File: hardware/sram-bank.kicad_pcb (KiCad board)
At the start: 2 copper layers, 50.8 x 78.7 mm, 45 parts, among them U1 74LVC138A, U10 74LVC8T245, U11 74LVC8T245, U12 IS66WV51216EALL, U13 74LVC138A, U2 74LVC8T245, U3 74LVC8T245, U4 74LVC8T245, U5 74LVC8T245, U6 74LVC8T245, U7 74LVC8T245, U8 74LVC8T245, U9 74LVC8T245

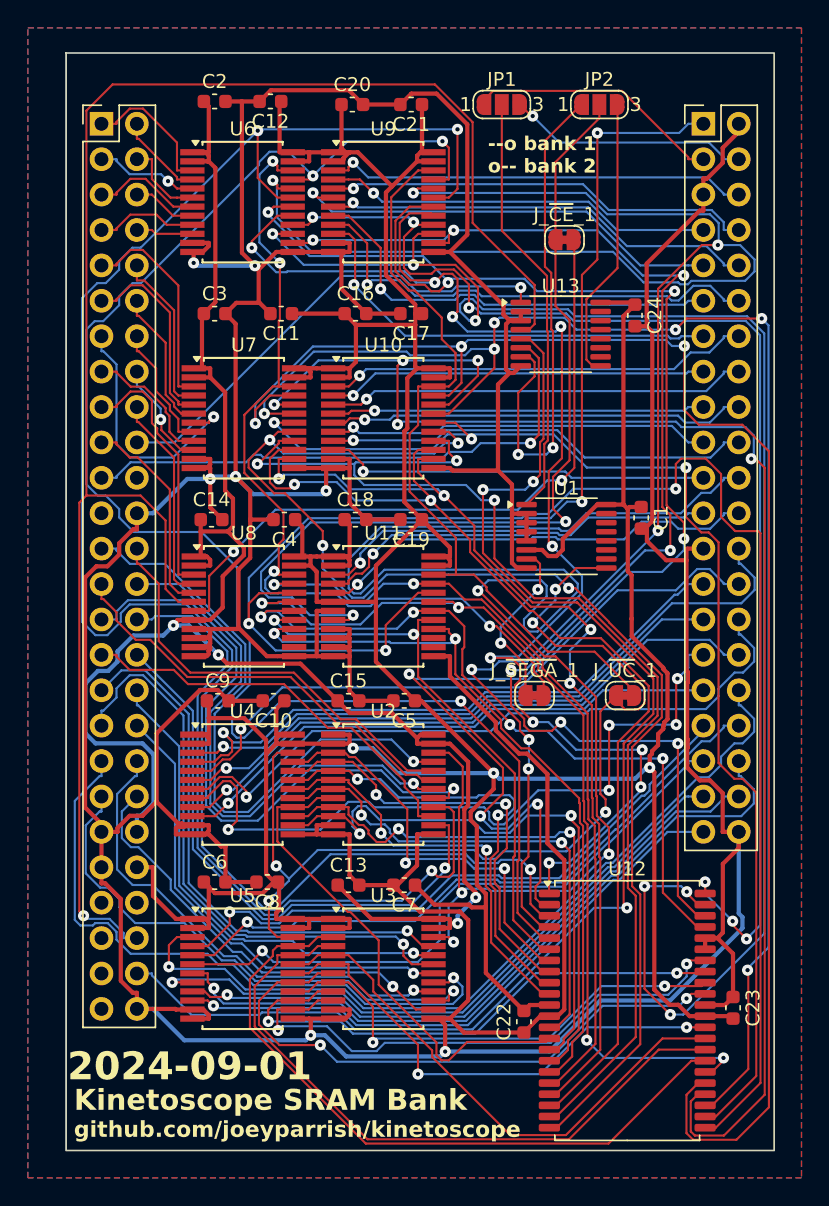
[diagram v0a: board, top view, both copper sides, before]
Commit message: Correct SRAM board debug pads
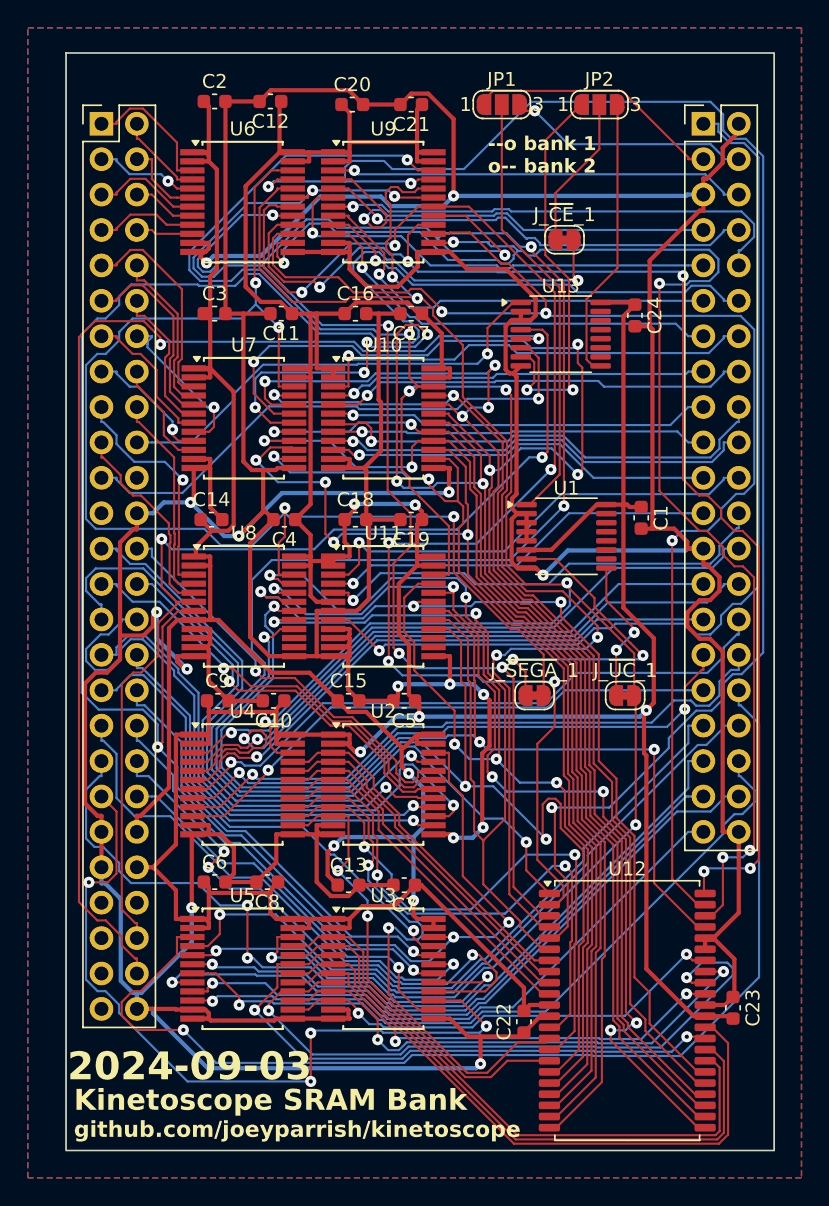
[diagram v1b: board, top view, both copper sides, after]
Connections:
- U2 pad 22: /~{SRAM_CE} -> /~{SRAM_CE_INT}
- U3 pad 22: /~{SRAM_CE} -> /~{SRAM_CE_INT}
- U4 pad 22: /~{UC_CONTROL} -> /~{UC_CONTROL_INT}
- U5 pad 22: /~{UC_CONTROL} -> /~{UC_CONTROL_INT}
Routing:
- net /~{SRAM_CE}: track 136.3 -> 11.0 mm, vias 5 -> 0
- net /~{UC_CONTROL_INT}: track 55.4 -> 172.6 mm, vias 0 -> 8
- net /~{SRAM_CE_INT}: track 49.4 -> 151.7 mm, vias 2 -> 4
- net /~{UC_CONTROL}: track 72.3 -> 10.5 mm, vias 5 -> 2
- net /~{SEGA_CE}: track 123.6 -> 74.1 mm, vias 1 -> 2
- net /SRAM_A17: track 115.7 -> 71.4 mm, vias 3 -> 6
- net /SRAM_A8: track 113.9 -> 74.1 mm, vias 3 -> 2
- net GND: track 503.0 -> 542.8 mm, vias 7 -> 15
- net /SRAM_A4: track 99.3 -> 139.0 mm, vias 10 -> 5
- net /SRAM_A1: track 133.1 -> 93.7 mm, vias 7 -> 4
- net /SRAM_A2: track 129.0 -> 90.6 mm, vias 3 -> 5
- net /~{SEGA_CONTROL_INT}: track 63.7 -> 95.2 mm
- net /~{SRAM_FINAL_WE}: track 53.5 -> 80.5 mm, vias 2 -> 3
- net /SRAM_A9: track 111.3 -> 85.2 mm, vias 5 -> 4
- net /SRAM_A12: track 96.4 -> 71.4 mm, vias 4 -> 2
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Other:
- board text added: "2024-09-03"
- board text removed: "2024-09-01"

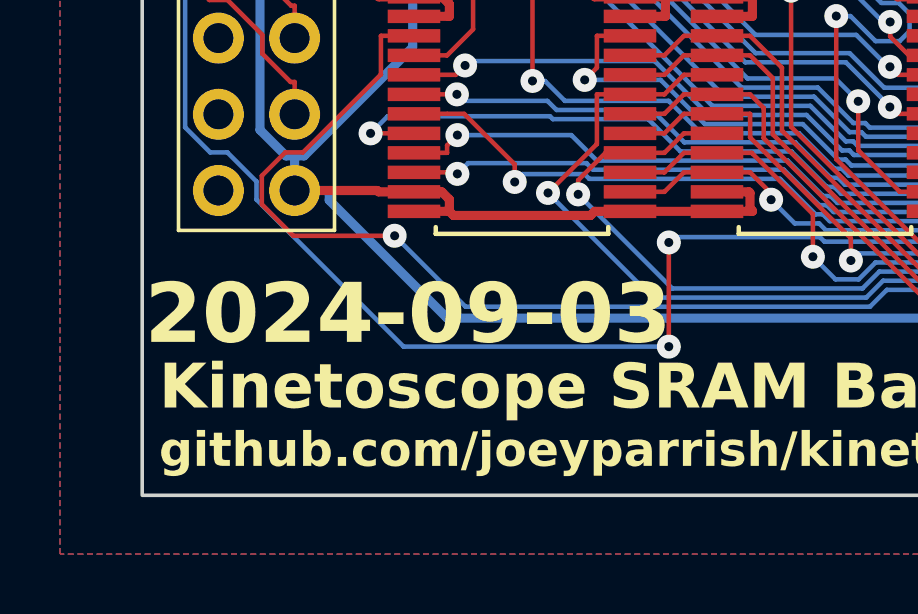
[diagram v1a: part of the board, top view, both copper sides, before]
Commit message: Fix footprint for new SMD regulator
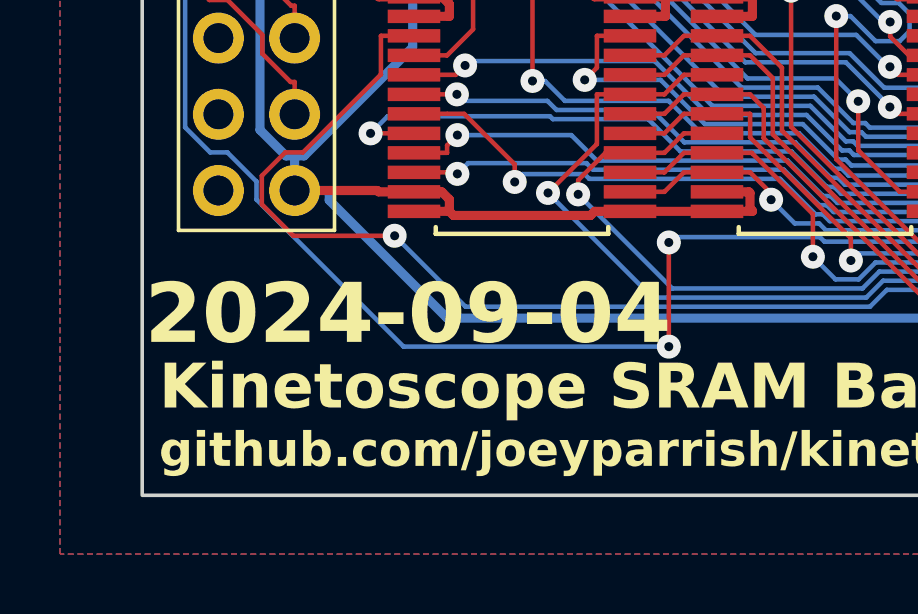
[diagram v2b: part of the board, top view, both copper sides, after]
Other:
- board text added: "2024-09-04"
- board text removed: "2024-09-03"
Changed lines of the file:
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@@
 				(type "Bottom Silk Screen")
 			)
-			(copper_finish "None")
 			(dielectric_constraints no)
 		)
@@
 		)
 	)
-	(gr_text "2024-09-03"
+	(gr_text "2024-09-04"
 		(at 27.6 92 0)
 		(layer "F.SilkS")
@@
 			)
 		)
-		(render_cache "2024-09-03" 0
+		(render_cache "2024-09-04" 0
 			(polygon
 				(pts
@@
 			(polygon
 				(pts
-					(xy 34.513538 90.829162) (xy 35.802163 90.829162) (xy 35.802163 91.098318) (xy 35.264829 91.642002)
-					(xy 35.498325 91.642002) (xy 35.802163 92.116322) (xy 35.802163 92.571591) (xy 35.554501 92.83)
-					(xy 34.513538 92.83) (xy 34.513538 92.585757) (xy 35.447522 92.585757) (xy 35.537892 92.496852)
-					(xy 35.537892 92.15247) (xy 35.35471 91.886245) (xy 34.940963 91.886245) (xy 34.940963 91.631256)
-					(xy 35.490021 91.073405) (xy 34.513538 91.073405)
+					(xy 35.717655 91.92337) (xy 35.886671 91.92337) (xy 35.886671 92.167613) (xy 35.717655 92.167613)
+					(xy 35.717655 92.83) (xy 35.450453 92.83) (xy 35.450453 92.167613) (xy 34.702093 92.167613) (xy 34.449984 91.797341)
+					(xy 34.735799 91.797341) (xy 34.823238 91.92337) (xy 35.450453 91.92337) (xy 35.450453 91.063147)
+					(xy 34.735799 91.797341) (xy 34.449984 91.797341) (xy 34.42903 91.766566) (xy 35.329309 90.829162)
+					(xy 35.717655 90.829162)
 				)
 			)

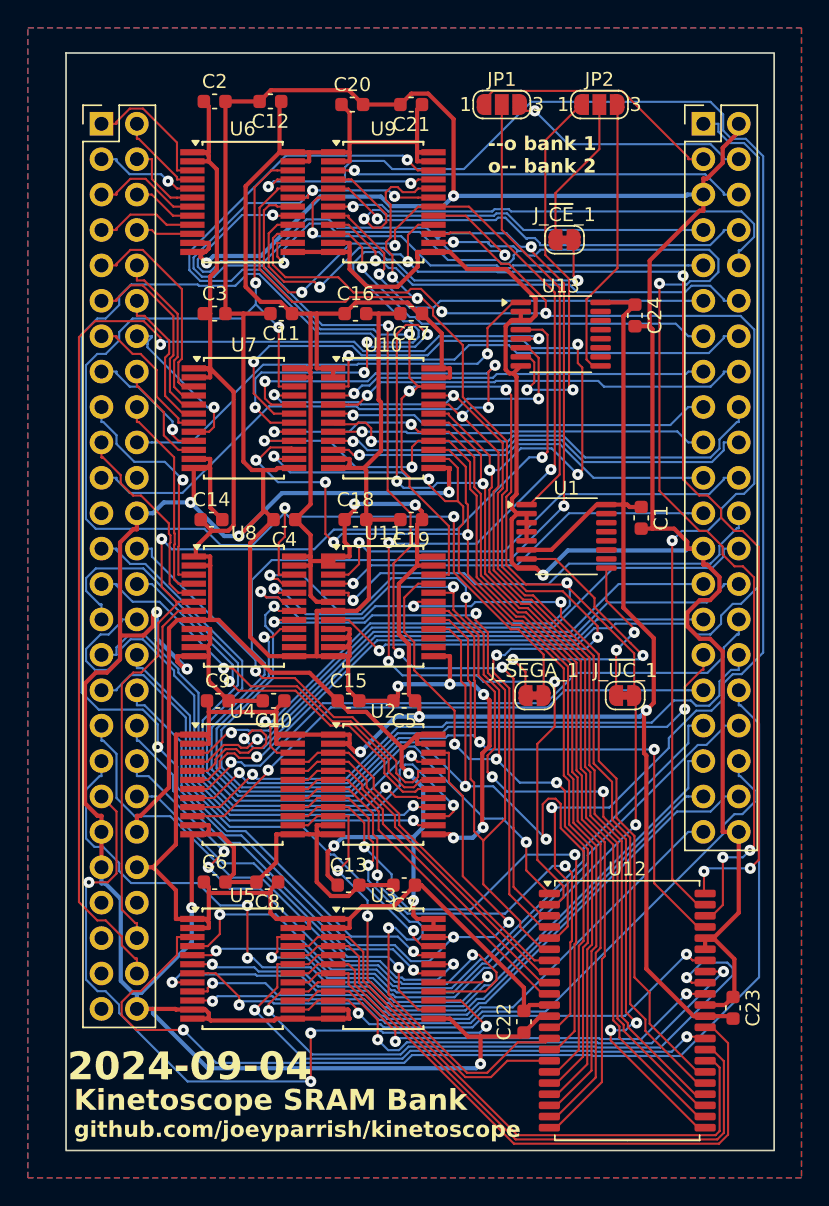
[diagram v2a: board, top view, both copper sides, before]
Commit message: Replace 8-bit buffers with cheaper version
Replace SN74LVC8T245DBR (8-bit buffers) with SN74LVC8T245PWR.  The old
version was SSOP, and the new version is a TSSOP size, but they are
otherwise the same.

This is estimated to reduce the price of a complete unit by over $11,
or about 16.5%.
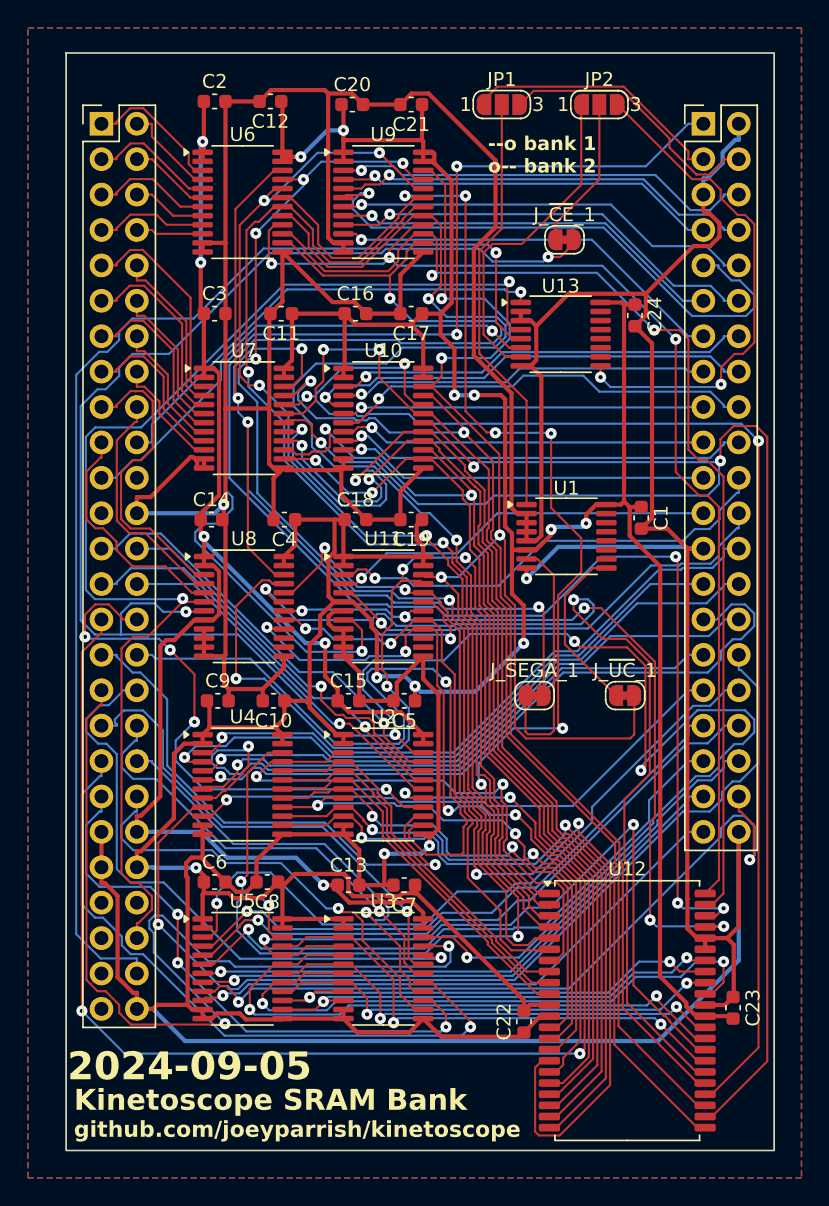
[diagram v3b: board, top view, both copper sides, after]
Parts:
- U10, U11, U2, U3, U4, U5, U6, U7, U8, U9: footprint Package_SO:SSOP-24_5.3x8.2mm_P0.65mm -> Package_SO:TSSOP-24_4.4x7.8mm_P0.65mm
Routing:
- net /SEGA_D4: track 44.9 -> 95.9 mm, vias 1 -> 4
- net GND: track 542.8 -> 492.6 mm, vias 15 -> 4
- net /SRAM_A4: track 139.0 -> 91.5 mm, vias 5 -> 2
- net /SRAM_A0: track 117.0 -> 83.2 mm, vias 3 -> 5
- net /SEGA_D8: track 35.4 -> 69.0 mm, vias 1 -> 2
- net /~{UC_CONTROL_INT}: track 172.6 -> 140.5 mm, vias 8 -> 7
- net /SRAM_A10: track 107.0 -> 75.6 mm, vias 4 -> 2
- net /SRAM_D_IN8: track 79.7 -> 51.2 mm
- net /SRAM_D_IN6: track 45.5 -> 70.5 mm
- net /~{SRAM_FINAL_WE}: track 80.5 -> 56.4 mm, vias 3 -> 4
- net /SRAM_DATA7: track 33.6 -> 57.4 mm
- net /SEGA_D7: track 29.7 -> 53.0 mm
- net /~{SRAM_FINAL_CE}: track 62.1 -> 41.1 mm
- net /SRAM_A3: track 99.6 -> 79.0 mm, vias 6 -> 2
- net /~{SRAM_CE_INT}: track 151.7 -> 172.1 mm, vias 4 -> 6
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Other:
- board text added: "2024-09-05"
- board text removed: "2024-09-04"

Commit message: Fix SRAM bank hardware design
 - Fix SRAM OE line (was previously CE by accident)
 - Fix buffer OE line
 - Add test pads for ~{SEGA_OE}, ~{SRAM_WE}, ~{SRAM_FINAL_OE}
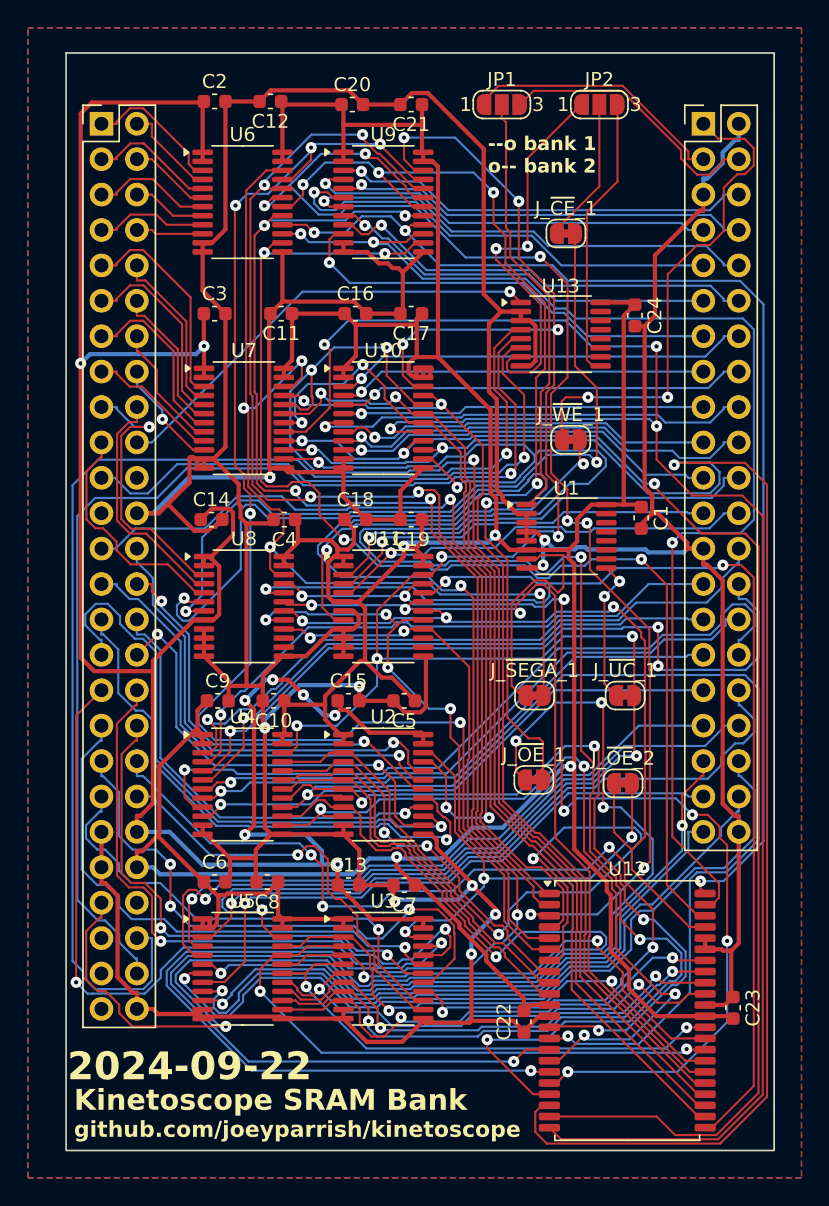
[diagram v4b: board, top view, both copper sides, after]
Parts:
- added J_~{OE}_1: ~, Jumper:SolderJumper-2_P1.3mm_Bridged_RoundedPad1.0x1.5mm, F.Cu at (52.3, 71.5)
- added J_~{OE}_2: ~, Jumper:SolderJumper-2_P1.3mm_Bridged_RoundedPad1.0x1.5mm, F.Cu at (58.7, 71.7)
- added J_~{WE}_1: ~, Jumper:SolderJumper-2_P1.3mm_Bridged_RoundedPad1.0x1.5mm, F.Cu at (55.0, 47.0)
- moved J_~{CE}_1 0.46 mm to (54.6, 32.2)
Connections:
- J1 pad 45: /kinetoscope-header-internal/~{SEGA_OE} -> /~{SEGA_OE}
- U11 pad 8: /~{SRAM_WE} -> /~{SRAM_WE_INT}
- U2 pad 22: /~{SRAM_CE_INT} -> /~{SRAM_OE_INT}
- U3 pad 22: /~{SRAM_CE_INT} -> /~{SRAM_OE_INT}
- U8 pad 6: /~{SEGA_CE} -> /~{SEGA_OE_INT}
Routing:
- net /~{SRAM_CE_INT}: track 172.1 -> 56.1 mm, vias 6 -> 2
- net /~{SEGA_OE}: track 0.00 -> 88.4 mm, vias 0 -> 4
- net GND: track 492.6 -> 423.6 mm, vias 4 -> 9
- net /SRAM_A15: track 64.9 -> 130.0 mm, vias 2 -> 5
- net /~{SEGA_OE_INT}: track 0.00 -> 65.0 mm, vias 0 -> 2
- net /SRAM_DATA6: track 37.6 -> 95.7 mm
- net /SEGA_D4: track 95.9 -> 40.0 mm, vias 4 -> 1
- net /SRAM_A12: track 80.3 -> 132.0 mm, vias 2 -> 4
- net +5V: track 110.3 -> 161.7 mm, vias 5 -> 8
- net /~{SRAM_WE}: track 81.6 -> 36.1 mm, vias 3 -> 2
- net /SRAM_A11: track 115.7 -> 74.8 mm, vias 3 -> 2
- net /SRAM_A14: track 72.1 -> 112.4 mm, vias 2 -> 3
- net /SRAM_DATA5: track 38.0 -> 78.2 mm
- net /SEGA_D13: track 32.7 -> 70.4 mm, vias 1 -> 5
- net /~{SRAM_FINAL_WE}: track 56.4 -> 93.9 mm
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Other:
- board text added: "2024-09-22"
- board text removed: "2024-09-05"
